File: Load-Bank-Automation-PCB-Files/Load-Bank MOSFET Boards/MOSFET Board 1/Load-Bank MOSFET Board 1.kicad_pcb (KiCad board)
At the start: 2 copper layers, 38.2 x 34 mm, 26 parts, among them J2 Conn_01x03, J22 Conn_01x03, Q22 GSGN0648, Q3 GSGN0648, U10 MCP6006-OTVAO, U3 ACS711xEXLT-31AB, U8 IRS10752LTRPBF

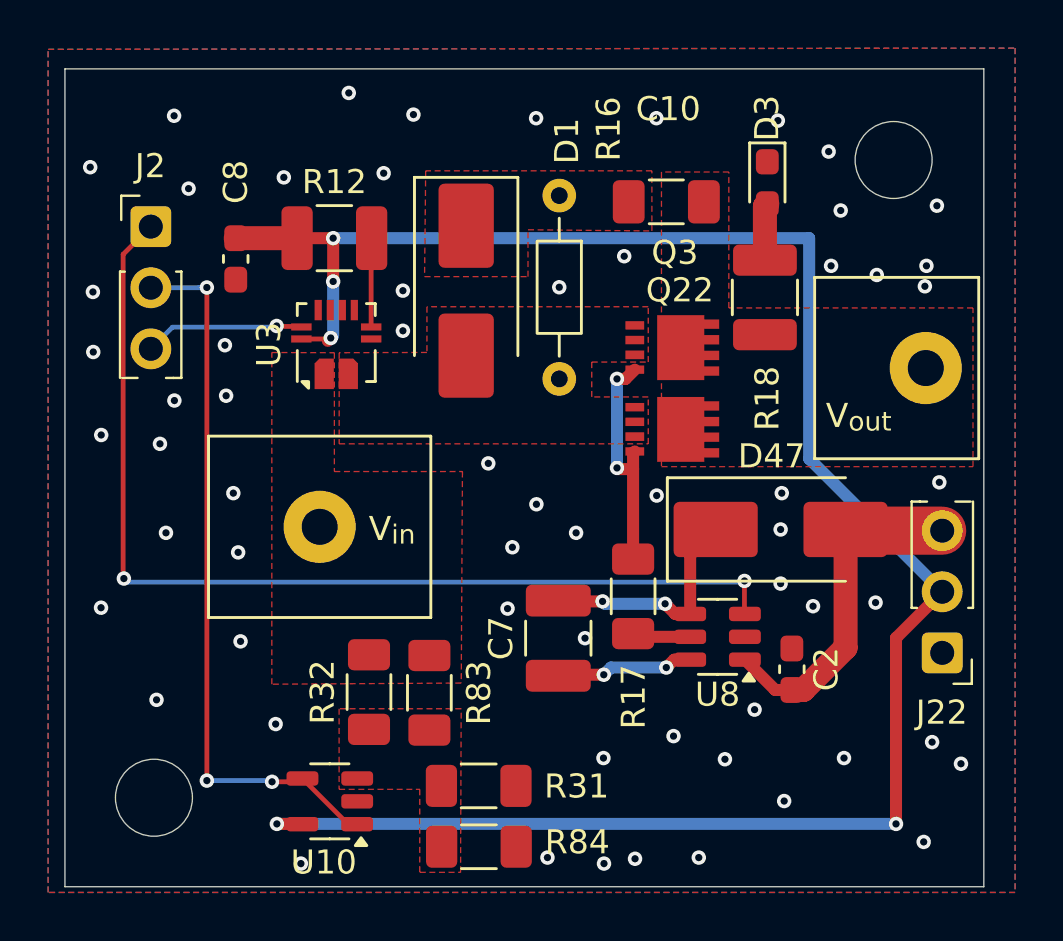
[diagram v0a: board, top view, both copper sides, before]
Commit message: MOSFET boards ready to be ordered
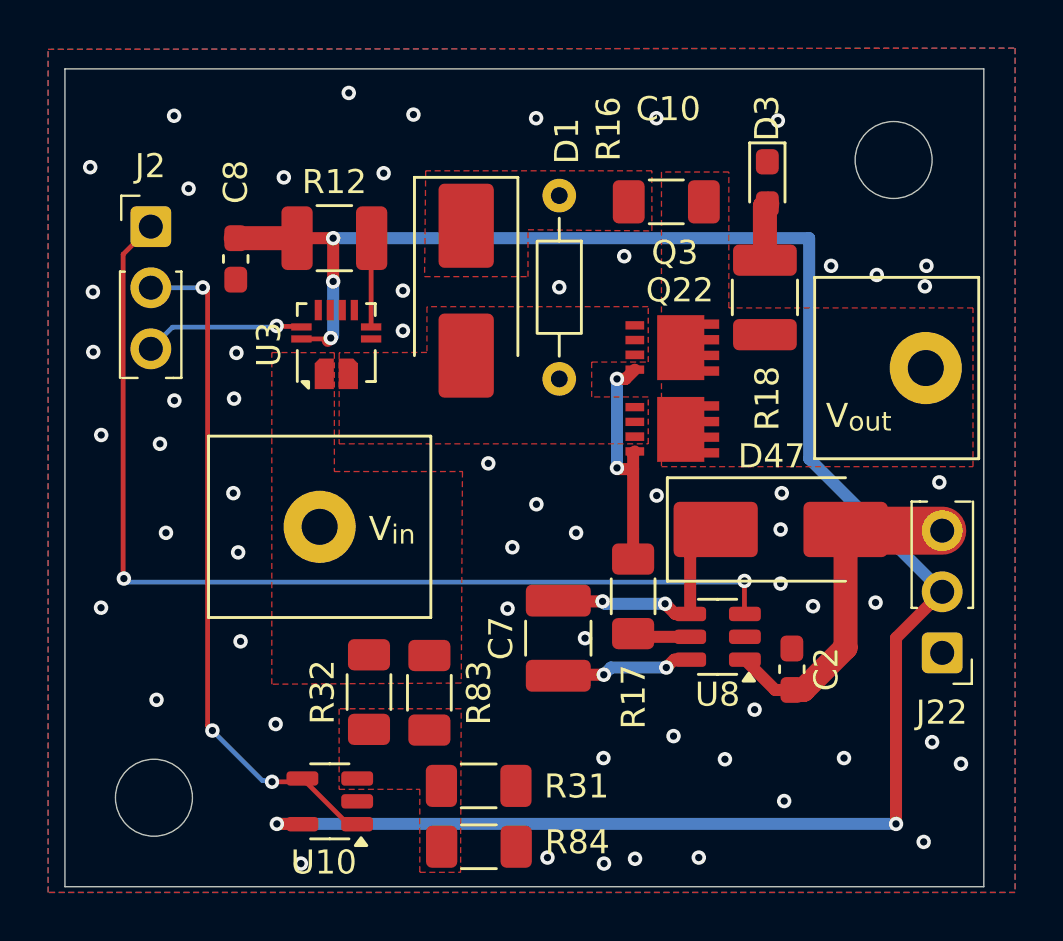
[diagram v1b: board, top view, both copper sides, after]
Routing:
- net /Mosfet Board 1/Voltage_ADC: track 30.1 -> 28.7 mm
- net GND: vias 62 -> 59
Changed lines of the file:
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@@
 			(drill 3.2)
 			(layers "*.Cu" "*.Mask")
+			(clearance 1.4)
 		)
 		(embedded_fonts no)
@@
 			(drill 3.2)
 			(layers "*.Cu" "*.Mask")
+			(clearance 1.4)
 		)
 		(embedded_fonts no)
@@
 	)
 	(via
-		(at 179.22 70.68)
-		(size 0.6)
-		(drill 0.3)
-		(layers "F.Cu" "B.Cu")
-		(capping no)
-		(covering
-			(front no)
-			(back no)
-		)
-		(plugging
-			(front no)
-			(back no)
-		)
-		(filling no)
-		(net "GND")
-	)
-	(via
 		(at 179.3575 93.4425)
 		(size 0.6)
@@
 	)
 	(via
-		(at 178.72 68.23)
-		(size 0.6)
-		(drill 0.3)
-		(layers "F.Cu" "B.Cu")
-		(capping no)
-		(covering
-			(front no)
-			(back no)
-		)
-		(plugging
-			(front no)
-			(back no)
-		)
-		(filling no)
-		(net "GND")
-	)
-	(via
 		(at 182.785 72.98)
 		(size 0.6)
@@
 	)
 	(via
-		(at 153.62 76.28)
+		(at 154.1 76.6)
 		(size 0.6)
 		(drill 0.3)
@@
 	)
 	(via
-		(at 153.67 78.38)
+		(at 154 78.5)
 		(size 0.6)
 		(drill 0.3)
@@
 	)
 	(via
-		(at 183.22 70.48)
-		(size 0.6)
-		(drill 0.3)
-		(layers "F.Cu" "B.Cu")
-		(capping no)
-		(covering
-			(front no)
-			(back no)
-		)
-		(plugging
-			(front no)
-			(back no)
-		)
-		(filling no)
-		(net "GND")
-	)
-	(via
 		(at 164.57 81.1925)
 		(size 0.6)
@@
 	)
 	(segment
-		(start 158.7425 96.1925)
-		(end 156.8425 94.2925)
+		(start 152.7 73.88)
+		(end 152.87 73.88)
 		(width 0.2)
 		(layer "F.Cu")
@@
 	)
 	(segment
-		(start 152.87 73.88)
-		(end 152.87 94.38)
+		(start 152.9 92.1)
+		(end 153.1 92.3)
+		(width 0.2)
+		(layer "F.Cu")
+		(net "/Mosfet Board 1/Voltage_ADC")
+	)
+	(segment
+		(start 158.7425 96.1925)
+		(end 156.8425 94.2925)
 		(width 0.2)
 		(layer "F.Cu")
@@
 		(net "/Mosfet Board 1/Voltage_ADC")
 	)
+	(segment
+		(start 152.9 73.91)
+		(end 152.9 92.1)
+		(width 0.2)
+		(layer "F.Cu")
+		(net "/Mosfet Board 1/Voltage_ADC")
+	)
+	(segment
+		(start 152.87 73.88)
+		(end 152.9 73.91)
+		(width 0.2)
+		(layer "F.Cu")
+		(net "/Mosfet Board 1/Voltage_ADC")
+	)
 	(via
 		(at 155.58 94.43)
@@
 	)
 	(via
-		(at 152.87 73.88)
+		(at 152.7 73.88)
 		(size 0.6)
 		(drill 0.3)
@@
 	)
 	(via
-		(at 152.87 94.38)
+		(at 153.1 92.3)
 		(size 0.6)
 		(drill 0.3)
@@
 	)
 	(segment
-		(start 152.57 73.88)
-		(end 152.56 73.89)
+		(start 155.53 94.38)
+		(end 155.58 94.43)
 		(width 0.2)
 		(layer "B.Cu")
@@
 	)
 	(segment
-		(start 152.87 94.38)
-		(end 155.53 94.38)
+		(start 152.7 73.88)
+		(end 152.57 73.88)
 		(width 0.2)
 		(layer "B.Cu")
@@
 	)
 	(segment
-		(start 152.87 73.88)
-		(end 152.57 73.88)
+		(start 152.56 73.89)
+		(end 150.54 73.89)
 		(width 0.2)
 		(layer "B.Cu")
@@
 	)
 	(segment
-		(start 155.53 94.38)
-		(end 155.58 94.43)
+		(start 155.18 94.38)
+		(end 155.53 94.38)
 		(width 0.2)
 		(layer "B.Cu")
@@
 	)
 	(segment
-		(start 152.56 73.89)
-		(end 150.54 73.89)
+		(start 153.1 92.3)
+		(end 155.18 94.38)
+		(width 0.2)
+		(layer "B.Cu")
+		(net "/Mosfet Board 1/Voltage_ADC")
+	)
+	(segment
+		(start 152.57 73.88)
+		(end 152.56 73.89)
 		(width 0.2)
 		(layer "B.Cu")
